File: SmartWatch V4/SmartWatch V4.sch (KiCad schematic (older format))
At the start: 64 parts, among them J1 10118192-0001LF, J10 TestPad, J11 TestPad, J12 TestPad, J13 TestPad, J14 TestPad, J2 , J3 TestPad, J4 TestPad, J5 TestPad, J6 TestPad, J7 TestPad, J8 TestPad, J9 TestPad, Q1 FDN340P, Q2 MMBT3904, Q3 MMBT3904, Q4 FDN340P, SW1 EVQ-P7J01P, SW2 EVQ-P7J01P, U1 MAX17048, U10 TSC2003IPWR, U11 NHD-1.8-128160EF-CTXI#-T, U2 FT231XS, U3 LP5912-3.3DRVT, U4 LP5912-2.8DRVT, U5 MCP73832-2-OT, U6 ESP32-WROOM-32, U7 NLSV4T244, U8 NLSV4T244, U9 NLSV4T244

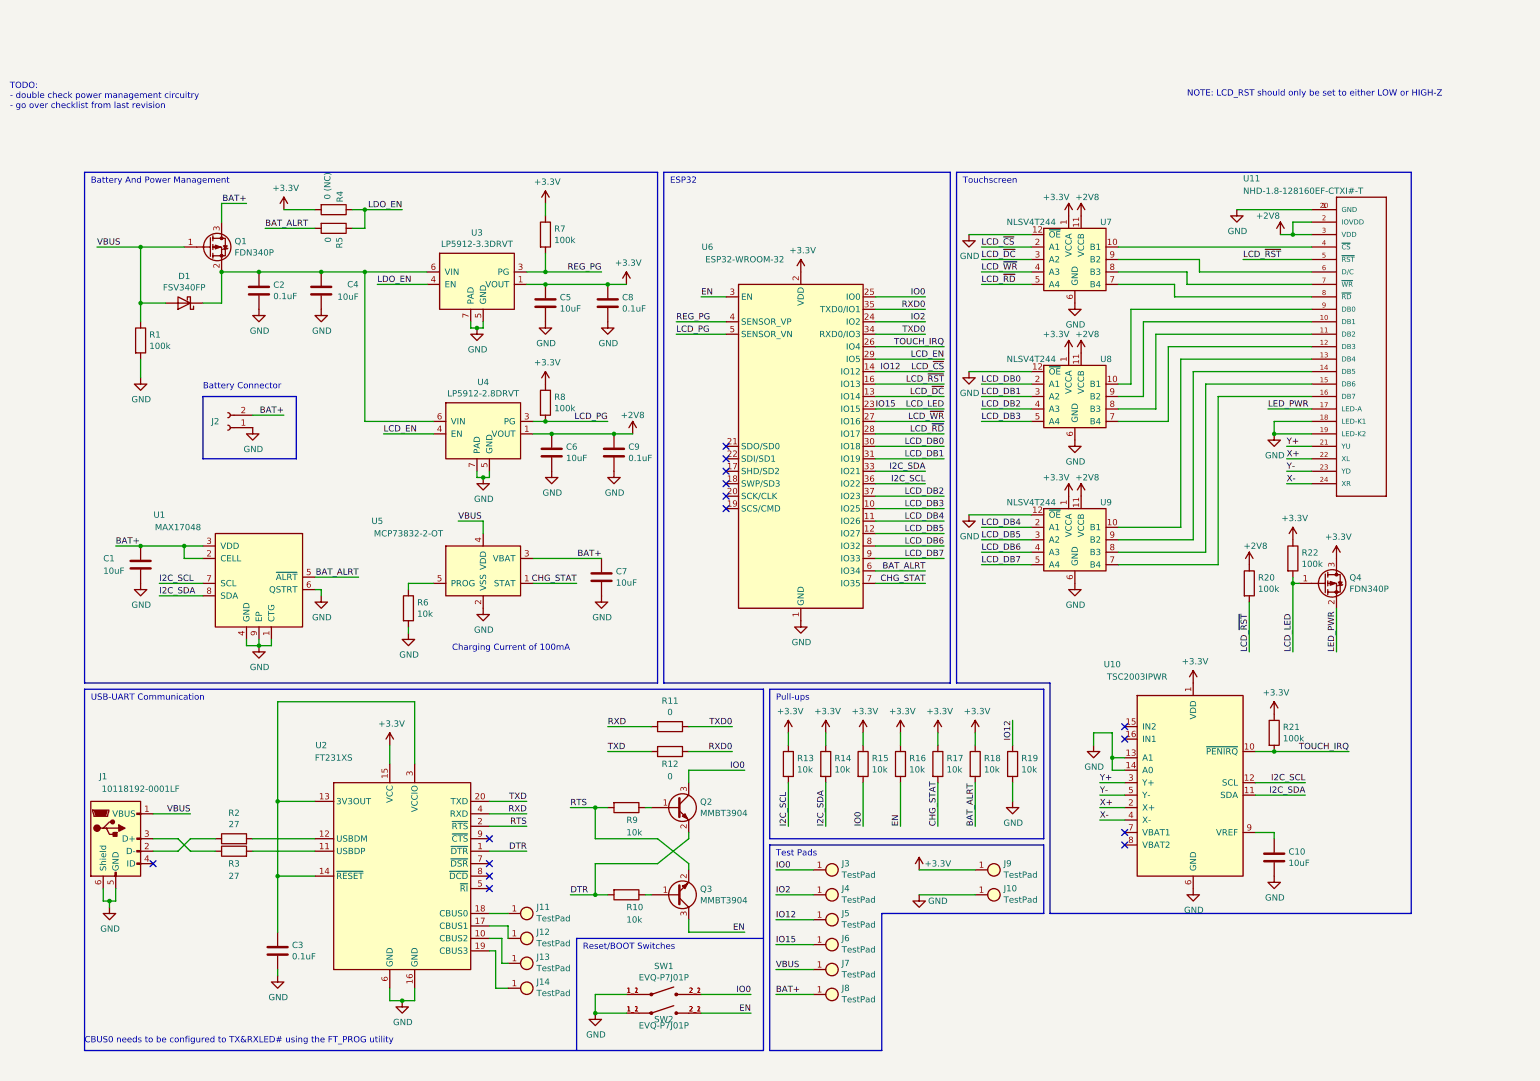
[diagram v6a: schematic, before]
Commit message: Completed work of schematic and board layout of revision 4
Also began work on new body for the watch
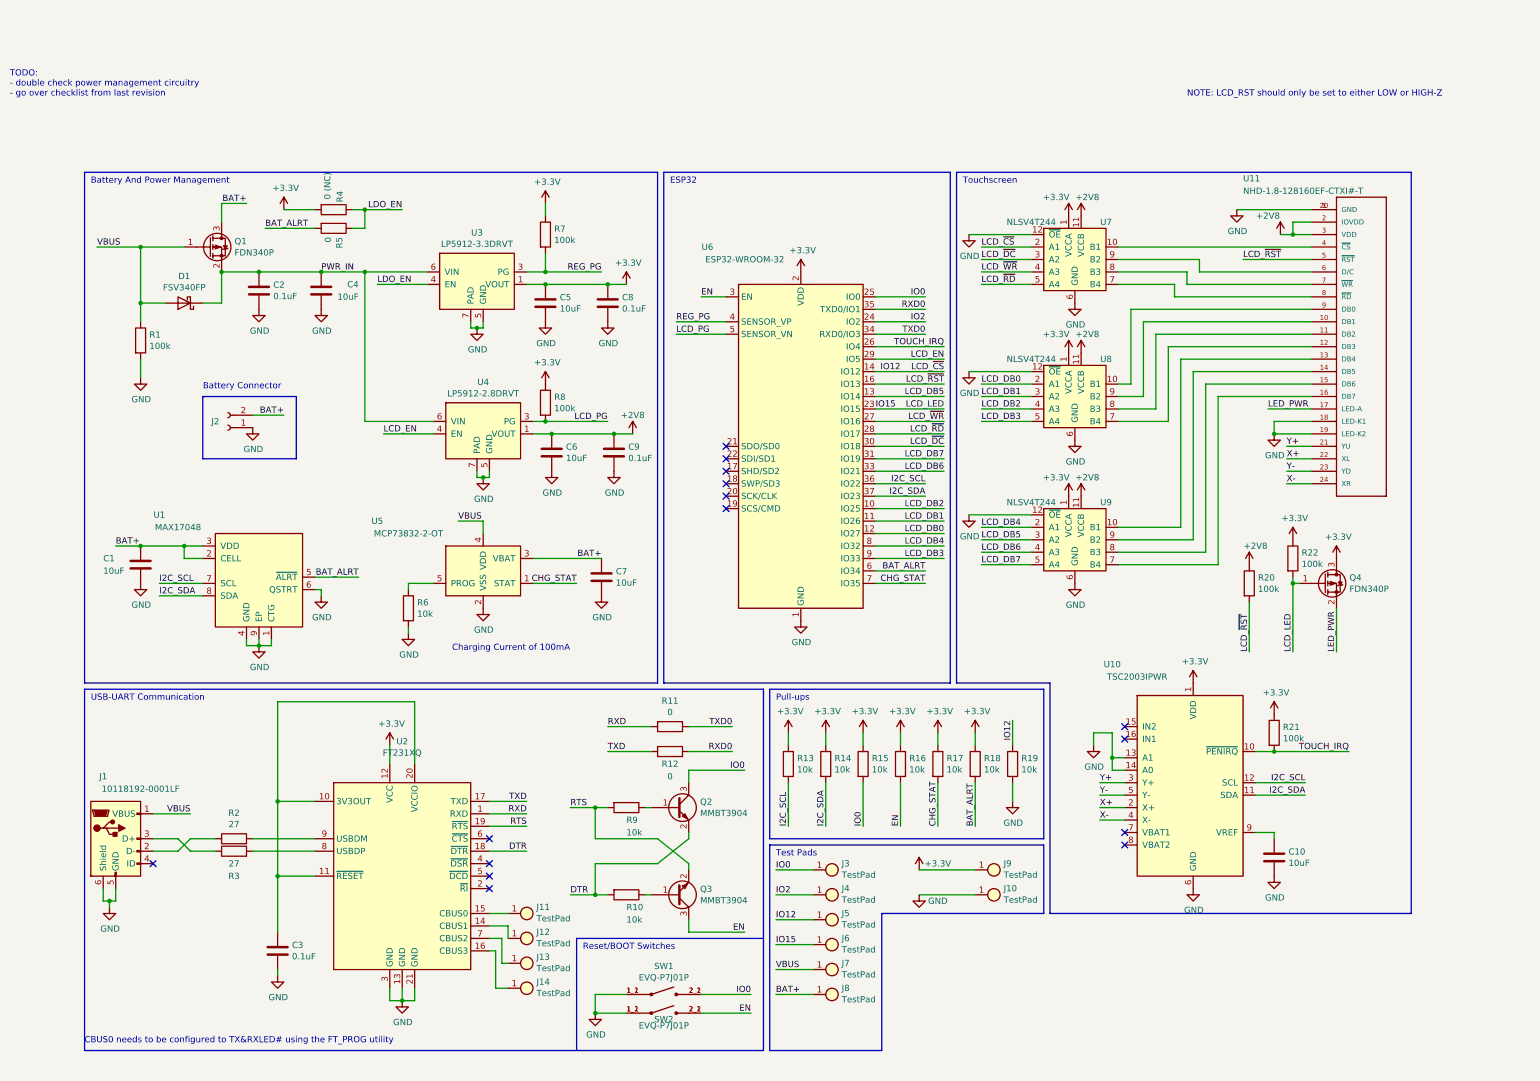
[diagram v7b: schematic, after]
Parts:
- removed U2: FT231XS, Package_SO:SSOP-20_3.9x8.7mm_P0.635mm, symbol Interface_USB:FT231XS
- added U2: FT231XQ, Package_DFN_QFN:QFN-20-1EP_4x4mm_P0.5mm_EP2.5x2.5mm, symbol Interface_USB:FT231XQ
- R2, R3: footprint Resistor_SMD:R_0805_2012Metric -> Resistor_SMD:R_0603_1608Metric; digikey 738-RMCF0805JT27R0CT-ND -> RMCF0603JT27R0CT-ND
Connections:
- net +3V3: now also U2.12 (VCC)
- net DTR: now also U2.18 (~DTR)
- net GND: now also U2.13 (GND), U2.21 (GND), U2.3 (GND)
- net I2C_SDA: now also U6.37 (IO23); no longer U6.33 (IO21)
- net LCD_DB0: now also U6.12 (IO27); no longer U6.30 (IO18)
- net LCD_DB1: now also U6.11 (IO26); no longer U6.31 (IO19)
- net LCD_DB2: now also U6.10 (IO25); no longer U6.37 (IO23)
- net LCD_DB3: now also U6.9 (IO33); no longer U6.10 (IO25)
- net LCD_DB4: now also U6.8 (IO32); no longer U6.11 (IO26)
- net LCD_DB5: now also U6.13 (IO14); no longer U6.12 (IO27)
- net LCD_DB6: now also U6.33 (IO21); no longer U6.8 (IO32)
- net LCD_DB7: now also U6.31 (IO19); no longer U6.9 (IO33)
- net LCD_~DC~: now also U6.30 (IO18); no longer U6.13 (IO14)
- net RTS: now also U2.19 (~RTS)
- net RXD: now also U2.1 (RXD)
- net TXD: now also U2.17 (TXD)
- net at R3.2: now also U2.8 (USBDP)
- net at J13.1: now also U2.7 (CBUS2)
- net at R2.2: now also U2.9 (USBDM)
- net at C3.1: now also U2.10 (3V3OUT), U2.11 (~RESET), U2.20 (VCCIO)
- net at J12.1: now also U2.14 (CBUS1)
- net at J11.1: now also U2.15 (CBUS0)
- net at J14.1: now also U2.16 (CBUS3)
- net PWR_IN: now reaches C2.1, C4.1, D1.1 (K), Q1.2 (S), U3.6 (VIN), U4.6 (VIN)
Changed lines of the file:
@@
 F 0 "R2" V 1957 5900 50  0000 C CNN
 F 1 "27" V 1866 5900 50  0000 C CNN
-F 2 "Resistor_SMD:R_0805_2012Metric" V 1680 5900 50  0001 C CNN
+F 2 "Resistor_SMD:R_0603_1608Metric" V 1680 5900 50  0001 C CNN
 F 3 "~" H 1750 5900 50  0001 C CNN
-F 4 "738-RMCF0805JT27R0CT-ND" V 1750 5900 50  0001 C CNN "digikey"
+F 4 "RMCF0603JT27R0CT-ND" V 1750 5900 50  0001 C CNN "digikey"
 	1    1750 5900
-	0    -1   -1   0
-$EndComp
-$Comp
-L Device:R R3
-U 1 1 5E6C4B82
-P 1750 6000
-F 0 "R3" V 1650 6000 50  0000 C CNN
-F 1 "27" V 1550 6000 50  0000 C CNN
-F 2 "Resistor_SMD:R_0805_2012Metric" V 1680 6000 50  0001 C CNN
-F 3 "~" H 1750 6000 50  0001 C CNN
-F 4 "738-RMCF0805JT27R0CT-ND" V 1750 6000 50  0001 C CNN "digikey"
-	1    1750 6000
 	0    -1   -1   0
 $EndComp
@@
 $EndComp
 Wire Wire Line
-	6900 2950 7300 2950
+	6900 3150 7300 3150
 Wire Wire Line
 	6900 3050 7300 3050
-Text Label 7300 2950 2    50   ~ 0
+Text Label 7300 3150 2    50   ~ 0
 I2C_SDA
 Text Label 7300 3050 2    50   ~ 0
@@
 	10250 1050 10400 1050
 Connection ~ 10250 1050
-Text Notes -50  50   0    50   ~ 0
+Text Notes -50  -50  0    50   ~ 0
 TODO: \n- double check power management circuitry\n- go over checklist from last revision
 Wire Wire Line
@@
 	6900 2250 7450 2250
 Wire Wire Line
-	6900 2750 7450 2750
-Wire Wire Line
-	6900 3150 7450 3150
+	6900 3450 7450 3450
 Wire Wire Line
 	6900 3250 7450 3250
 Wire Wire Line
-	6900 3350 7450 3350
+	6900 3650 7450 3650
 Wire Wire Line
 	6900 3550 7450 3550
 Wire Wire Line
-	6900 3650 7450 3650
+	6900 2950 7450 2950
+Wire Wire Line
+	6900 2850 7450 2850
 Text Label 7450 2150 2    50   ~ 0
 LCD_~CS~
 Text Label 7450 2250 2    50   ~ 0
 LCD_~RST~
+Text Label 7450 3450 2    50   ~ 0
+LCD_DB0
+Text Label 7450 3250 2    50   ~ 0
+LCD_DB2
+Text Label 7450 3650 2    50   ~ 0
+LCD_DB3
+Text Label 7450 3550 2    50   ~ 0
+LCD_DB4
+Text Label 7450 2950 2    50   ~ 0
+LCD_DB6
+Text Label 7450 2850 2    50   ~ 0
+LCD_DB7
 Text Label 7450 2750 2    50   ~ 0
-LCD_DB0
-Text Label 7450 3150 2    50   ~ 0
-LCD_DB2
-Text Label 7450 3250 2    50   ~ 0
-LCD_DB3
+LCD_~DC~
+Wire Wire Line
+	6900 2750 7450 2750
+Text Label 7450 2350 2    50   ~ 0
+LCD_DB5
+Wire Wire Line
+	6900 2350 7450 2350
 Text Label 7450 3350 2    50   ~ 0
-LCD_DB4
-Text Label 7450 3550 2    50   ~ 0
-LCD_DB6
-Text Label 7450 3650 2    50   ~ 0
-LCD_DB7
-Text Label 7450 2650 2    50   ~ 0
-LCD_~RD~
-Text Label 7450 2550 2    50   ~ 0
-LCD_~WR~
-Text Label 7450 2350 2    50   ~ 0
-LCD_~DC~
-Wire Wire Line
-	6900 2650 7450 2650
-Wire Wire Line
-	6900 2550 7450 2550
-Wire Wire Line
-	6900 2350 7450 2350
-Text Label 7450 3450 2    50   ~ 0
-LCD_DB5
-Wire Wire Line
-	6900 3450 7450 3450
-Text Label 7450 2850 2    50   ~ 0
 LCD_DB1
 Wire Wire Line
-	6900 2850 7450 2850
+	6900 3350 7450 3350
 Wire Bus Line
 	5150 550  5150 4650
@@
 IO15
 $Comp
-L Interface_USB:FT231XS U2
-U 1 1 5E6D1202
-P 3100 6200
-F 0 "U2" H 2450 7250 50  0000 C CNN
-F 1 "FT231XS" H 2550 7150 50  0000 C CNN
-F 2 "Package_SO:SSOP-20_3.9x8.7mm_P0.635mm" H 4100 5400 50  0001 C CNN
-F 3 "https://www.ftdichip.com/Support/Documents/DataSheets/ICs/DS_FT231X.pdf" H 3100 6200 50  0001 C CNN
-F 4 "768-1129-1-ND" H 3100 6200 50  0001 C CNN "digikey"
-	1    3100 6200
-	1    0    0    -1
-$EndComp
-$Comp
 L CustomParts:TestPad J12
 U 1 1 5F244C41
@@
 	1    0    0    -1
 $EndComp
+$Comp
+L Interface_USB:FT231XQ U2
+U 1 1 5EAC2083
+P 3100 6200
+F 0 "U2" H 3100 7281 50  0000 C CNN
+F 1 "FT231XQ" H 3100 7190 50  0000 C CNN
+F 2 "Package_DFN_QFN:QFN-20-1EP_4x4mm_P0.5mm_EP2.5x2.5mm" H 4450 5400 50  0001 C CNN
+F 3 "https://www.ftdichip.com/Support/Documents/DataSheets/ICs/DS_FT231X.pdf" H 3100 6200 50  0001 C CNN
+F 4 "768-1128-1-ND" H 3100 6200 50  0001 C CNN "digikey"
+	1    3100 6200
+	1    0    0    -1
+$EndComp
+Wire Wire Line
+	3100 7100 3100 7200
+$Comp
+L Device:R R3
+U 1 1 5EAC0FC6
+P 1750 6000
+F 0 "R3" V 1550 6000 50  0000 C CNN
+F 1 "27" V 1650 6000 50  0000 C CNN
+F 2 "Resistor_SMD:R_0603_1608Metric" V 1680 6000 50  0001 C CNN
+F 3 "~" H 1750 6000 50  0001 C CNN
+F 4 "RMCF0603JT27R0CT-ND" V 1750 6000 50  0001 C CNN "digikey"
+	1    1750 6000
+	0    -1   -1   0
+$EndComp
+Wire Wire Line
+	6900 2550 7450 2550
+Wire Wire Line
+	6900 2650 7450 2650
+Text Label 7450 2550 2    50   ~ 0
+LCD_~WR~
+Text Label 7450 2650 2    50   ~ 0
+LCD_~RD~
+Text Label 2450 1350 0    50   ~ 0
+PWR_IN
 $EndSCHEMATC
